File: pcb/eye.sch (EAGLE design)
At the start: 36 parts, among them U1 WS2812, U10 WS2812, U11 WS2812, U12 WS2812, U13 WS2812, U14 WS2812, U15 WS2812, U16 WS2812, U17 WS2812, U18 WS2812, U19 WS2812, U2 WS2812, U20 WS2812, U21 WS2812, U22 WS2812, U23 WS2812, U24 WS2812, U25 WS2812, U26 WS2812, U27 WS2812, U28 WS2812, U29 WS2812, U3 WS2812, U30 WS2812, U4 WS2812, U5 WS2812, U6 WS2812, U7 WS2812, U8 WS2812, U9 WS2812

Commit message: start route data lines
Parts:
- added J1, J2: 3-PIN SMD, SparkFun-Connectors:CONN_03JST-SMD
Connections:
- new net N$30: J1.2, U1.DI
- net +5V: now also J1.3, J2.3
- net GND: now also J1.1, J2.1
- net N$31: now also J2.2
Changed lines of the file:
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@@
 <part name="P+36" library="supply1" library_urn="urn:adsk.eagle:library:371" deviceset="+5V" device=""/>
 <part name="GND36" library="supply1" library_urn="urn:adsk.eagle:library:371" deviceset="GND" device=""/>
+<part name="J1" library="SparkFun-Connectors" library_urn="urn:adsk.eagle:library:513" deviceset="CONN_03" device="JST-SMD" package3d_urn="urn:adsk.eagle:package:38075/1" value="3-PIN SMD"/>
+<part name="P+37" library="supply1" library_urn="urn:adsk.eagle:library:371" deviceset="+5V" device=""/>
+<part name="GND37" library="supply1" library_urn="urn:adsk.eagle:library:371" deviceset="GND" device=""/>
+<part name="J2" library="SparkFun-Connectors" library_urn="urn:adsk.eagle:library:513" deviceset="CONN_03" device="JST-SMD" package3d_urn="urn:adsk.eagle:package:38075/1" value="3-PIN SMD"/>
+<part name="GND38" library="supply1" library_urn="urn:adsk.eagle:library:371" deviceset="GND" device=""/>
+<part name="P+38" library="supply1" library_urn="urn:adsk.eagle:library:371" deviceset="+5V" device=""/>
 </parts>
 <sheets>
@@
 <attribute name="VALUE" x="261.62" y="83.82" size="1.778" layer="96"/>
 </instance>
+<instance part="J1" gate="J$1" x="-10.16" y="215.9" smashed="yes">
+<attribute name="VALUE" x="-12.7" y="208.534" size="1.778" layer="96" font="vector"/>
+<attribute name="NAME" x="-12.7" y="221.488" size="1.778" layer="95" font="vector"/>
+</instance>
+<instance part="P+37" gate="1" x="5.08" y="220.98" smashed="yes">
+<attribute name="VALUE" x="5.08" y="220.98" size="1.778" layer="96"/>
+</instance>
+<instance part="GND37" gate="1" x="5.08" y="210.82" smashed="yes">
+<attribute name="VALUE" x="2.54" y="208.28" size="1.778" layer="96"/>
+</instance>
+<instance part="J2" gate="J$1" x="266.7" y="71.12" smashed="yes" rot="R180">
+<attribute name="VALUE" x="261.62" y="63.754" size="1.778" layer="96" font="vector"/>
+<attribute name="NAME" x="266.7" y="76.708" size="1.778" layer="95" font="vector"/>
+</instance>
+<instance part="GND38" gate="1" x="254" y="76.2" smashed="yes">
+<attribute name="VALUE" x="251.46" y="73.66" size="1.778" layer="96"/>
+</instance>
+<instance part="P+38" gate="1" x="254" y="68.58" smashed="yes">
+<attribute name="VALUE" x="254" y="68.58" size="1.778" layer="96"/>
+</instance>
 </instances>
 <busses>
@@
 <pinref part="P+36" gate="1" pin="+5V"/>
 </segment>
+<segment>
+<pinref part="J1" gate="J$1" pin="3"/>
+<pinref part="P+37" gate="1" pin="+5V"/>
+<wire x1="5.08" y1="218.44" x2="-2.54" y2="218.44" width="0.1524" layer="91"/>
+</segment>
+<segment>
+<pinref part="J2" gate="J$1" pin="3"/>
+<pinref part="P+38" gate="1" pin="+5V"/>
+<wire x1="254" y1="66.04" x2="259.08" y2="66.04" width="0.1524" layer="91"/>
+<wire x1="259.08" y1="66.04" x2="259.08" y2="68.58" width="0.1524" layer="91"/>
+</segment>
 </net>
 <net name="GND" class="0">
@@
 <pinref part="C6" gate="G$1" pin="2"/>
 <pinref part="GND36" gate="1" pin="GND"/>
+</segment>
+<segment>
+<pinref part="J1" gate="J$1" pin="1"/>
+<pinref part="GND37" gate="1" pin="GND"/>
+<wire x1="5.08" y1="213.36" x2="-2.54" y2="213.36" width="0.1524" layer="91"/>
+</segment>
+<segment>
+<pinref part="J2" gate="J$1" pin="1"/>
+<pinref part="GND38" gate="1" pin="GND"/>
+<wire x1="254" y1="78.74" x2="259.08" y2="78.74" width="0.1524" layer="91"/>
+<wire x1="259.08" y1="78.74" x2="259.08" y2="73.66" width="0.1524" layer="91"/>
 </segment>
 </net>
@@
 <segment>
 <pinref part="U30" gate="U1" pin="DO"/>
-<wire x1="248.92" y1="88.9" x2="248.92" y2="81.28" width="0.1524" layer="91"/>
-</segment>
-</net>
+<pinref part="J2" gate="J$1" pin="2"/>
+<wire x1="248.92" y1="88.9" x2="248.92" y2="71.12" width="0.1524" layer="91"/>
+<wire x1="248.92" y1="71.12" x2="259.08" y2="71.12" width="0.1524" layer="91"/>
+</segment>
+</net>
+<net name="N$30" class="0">
+<segment>
+<pinref part="J1" gate="J$1" pin="2"/>
+<pinref part="U1" gate="U1" pin="DI"/>
+<wire x1="-2.54" y1="215.9" x2="22.86" y2="215.9" width="0.1524" layer="91"/>
+</segment>
+</net>

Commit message: change connector to TE AMP 171826-3
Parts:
- removed J1, J2: 3-PIN SMD, SparkFun-Connectors:CONN_03JST-SMD
- added JP1, JP2: (no value), pinhead:PINHD-1X3/90
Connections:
- net +5V: now also JP1.3, JP2.3; no longer J1.3, J2.3
- net GND: now also JP1.1, JP2.1; no longer J1.1, J2.1
- net N$30: now also JP1.2; no longer J1.2
- net N$31: now also JP2.2; no longer J2.2
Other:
- note added: "AMP171826-3"
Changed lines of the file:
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@@
 <part name="P+36" library="supply1" library_urn="urn:adsk.eagle:library:371" deviceset="+5V" device=""/>
 <part name="GND36" library="supply1" library_urn="urn:adsk.eagle:library:371" deviceset="GND" device=""/>
-<part name="J1" library="SparkFun-Connectors" library_urn="urn:adsk.eagle:library:513" deviceset="CONN_03" device="JST-SMD" package3d_urn="urn:adsk.eagle:package:38075/1" value="3-PIN SMD"/>
 <part name="P+37" library="supply1" library_urn="urn:adsk.eagle:library:371" deviceset="+5V" device=""/>
 <part name="GND37" library="supply1" library_urn="urn:adsk.eagle:library:371" deviceset="GND" device=""/>
-<part name="J2" library="SparkFun-Connectors" library_urn="urn:adsk.eagle:library:513" deviceset="CONN_03" device="JST-SMD" package3d_urn="urn:adsk.eagle:package:38075/1" value="3-PIN SMD"/>
 <part name="GND38" library="supply1" library_urn="urn:adsk.eagle:library:371" deviceset="GND" device=""/>
 <part name="P+38" library="supply1" library_urn="urn:adsk.eagle:library:371" deviceset="+5V" device=""/>
+<part name="JP1" library="pinhead" library_urn="urn:adsk.eagle:library:325" deviceset="PINHD-1X3" device="/90" package3d_urn="urn:adsk.eagle:package:22459/2"/>
+<part name="JP2" library="pinhead" library_urn="urn:adsk.eagle:library:325" deviceset="PINHD-1X3" device="/90" package3d_urn="urn:adsk.eagle:package:22459/2"/>
 </parts>
 <sheets>
 <sheet>
 <plain>
+<text x="0" y="208.28" size="1.778" layer="91" rot="R90">AMP171826-3</text>
+<text x="271.78" y="63.5" size="1.778" layer="91" rot="R90">AMP171826-3</text>
 </plain>
 <instances>
@@
 <attribute name="VALUE" x="261.62" y="83.82" size="1.778" layer="96"/>
 </instance>
-<instance part="J1" gate="J$1" x="-10.16" y="215.9" smashed="yes">
-<attribute name="VALUE" x="-12.7" y="208.534" size="1.778" layer="96" font="vector"/>
-<attribute name="NAME" x="-12.7" y="221.488" size="1.778" layer="95" font="vector"/>
-</instance>
-<instance part="P+37" gate="1" x="5.08" y="220.98" smashed="yes">
-<attribute name="VALUE" x="5.08" y="220.98" size="1.778" layer="96"/>
-</instance>
-<instance part="GND37" gate="1" x="5.08" y="210.82" smashed="yes">
-<attribute name="VALUE" x="2.54" y="208.28" size="1.778" layer="96"/>
-</instance>
-<instance part="J2" gate="J$1" x="266.7" y="71.12" smashed="yes" rot="R180">
-<attribute name="VALUE" x="261.62" y="63.754" size="1.778" layer="96" font="vector"/>
-<attribute name="NAME" x="266.7" y="76.708" size="1.778" layer="95" font="vector"/>
+<instance part="P+37" gate="1" x="12.7" y="220.98" smashed="yes">
+<attribute name="VALUE" x="12.7" y="220.98" size="1.778" layer="96"/>
+</instance>
+<instance part="GND37" gate="1" x="12.7" y="210.82" smashed="yes">
+<attribute name="VALUE" x="10.16" y="208.28" size="1.778" layer="96"/>
 </instance>
 <instance part="GND38" gate="1" x="254" y="76.2" smashed="yes">
@@
 <instance part="P+38" gate="1" x="254" y="68.58" smashed="yes">
 <attribute name="VALUE" x="254" y="68.58" size="1.778" layer="96"/>
+</instance>
+<instance part="JP1" gate="A" x="2.54" y="215.9" smashed="yes" rot="R180">
+<attribute name="NAME" x="6.35" y="210.185" size="1.778" layer="95" rot="R180"/>
+<attribute name="VALUE" x="8.89" y="223.52" size="1.778" layer="96" rot="R180"/>
+</instance>
+<instance part="JP2" gate="A" x="266.7" y="71.12" smashed="yes">
+<attribute name="NAME" x="260.35" y="76.835" size="1.778" layer="95"/>
+<attribute name="VALUE" x="260.35" y="63.5" size="1.778" layer="96"/>
 </instance>
 </instances>
@@
 </segment>
 <segment>
-<pinref part="J1" gate="J$1" pin="3"/>
 <pinref part="P+37" gate="1" pin="+5V"/>
-<wire x1="5.08" y1="218.44" x2="-2.54" y2="218.44" width="0.1524" layer="91"/>
-</segment>
-<segment>
-<pinref part="J2" gate="J$1" pin="3"/>
+<wire x1="12.7" y1="218.44" x2="5.08" y2="218.44" width="0.1524" layer="91"/>
+<pinref part="JP1" gate="A" pin="3"/>
+</segment>
+<segment>
 <pinref part="P+38" gate="1" pin="+5V"/>
 <wire x1="254" y1="66.04" x2="259.08" y2="66.04" width="0.1524" layer="91"/>
 <wire x1="259.08" y1="66.04" x2="259.08" y2="68.58" width="0.1524" layer="91"/>
+<wire x1="259.08" y1="68.58" x2="264.16" y2="68.58" width="0.1524" layer="91"/>
+<pinref part="JP2" gate="A" pin="3"/>
 </segment>
 </net>
@@
 </segment>
 <segment>
-<pinref part="J1" gate="J$1" pin="1"/>
 <pinref part="GND37" gate="1" pin="GND"/>
-<wire x1="5.08" y1="213.36" x2="-2.54" y2="213.36" width="0.1524" layer="91"/>
-</segment>
-<segment>
-<pinref part="J2" gate="J$1" pin="1"/>
+<wire x1="12.7" y1="213.36" x2="5.08" y2="213.36" width="0.1524" layer="91"/>
+<pinref part="JP1" gate="A" pin="1"/>
+</segment>
+<segment>
 <pinref part="GND38" gate="1" pin="GND"/>
 <wire x1="254" y1="78.74" x2="259.08" y2="78.74" width="0.1524" layer="91"/>
 <wire x1="259.08" y1="78.74" x2="259.08" y2="73.66" width="0.1524" layer="91"/>
+<wire x1="259.08" y1="73.66" x2="264.16" y2="73.66" width="0.1524" layer="91"/>
+<pinref part="JP2" gate="A" pin="1"/>
 </segment>
 </net>
@@
 <segment>
 <pinref part="U30" gate="U1" pin="DO"/>
-<pinref part="J2" gate="J$1" pin="2"/>
 <wire x1="248.92" y1="88.9" x2="248.92" y2="71.12" width="0.1524" layer="91"/>
-<wire x1="248.92" y1="71.12" x2="259.08" y2="71.12" width="0.1524" layer="91"/>
+<wire x1="248.92" y1="71.12" x2="264.16" y2="71.12" width="0.1524" layer="91"/>
+<pinref part="JP2" gate="A" pin="2"/>
 </segment>
 </net>
 <net name="N$30" class="0">
 <segment>
-<pinref part="J1" gate="J$1" pin="2"/>
 <pinref part="U1" gate="U1" pin="DI"/>
-<wire x1="-2.54" y1="215.9" x2="22.86" y2="215.9" width="0.1524" layer="91"/>
-</segment>
-</net>
+<wire x1="5.08" y1="215.9" x2="22.86" y2="215.9" width="0.1524" layer="91"/>
+<pinref part="JP1" gate="A" pin="2"/>
+</segment>
+</net>

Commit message: make full glasses and add mcu to them
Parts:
- removed JP2: (no value), pinhead:PINHD-1X3/90
- added 32U4: 32U4, SparkFun-IC-Microcontroller:ATMEGA32U4QFN
- added C10, C11, C12, C7, C8, C9: (no value), rcl:C-EUC0805
- added C13, C14: 1u, rcl:C-EUC0805
- added C15, C16: 20p, rcl:C-EUC0805
- added J1: (no value), SparkFun-Connectors:USB_MICRO-B_FEMALE-SMT
- added Q1: ECS-160-20-3X-TR, SparkFun-Clocks:CRYSTALSMD-3.2X1.5
- added R1: 470, rcl:R-US_R0805
- added R2, R3: 22, rcl:R-US_R0805
- added R4: 1k, rcl:R-US_R0805
- added U31, U32, U33, U34, U35, U36, U37, U38, U39, U40, U41, U42, U43, U44, U45, U46, U47, U48, U49, U50, U51, U52, U53, U54, U55, U56, U57, U58, U59, U60: WS2812, SparkFun-LED:WS2812"
- JP1: value (none) -> JST-ZH-5; device pinhead:PINHD-1X3/90 -> josh:JST-ZH-5
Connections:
- new net LED_DATA: 32U4.PB7, R1.1
- new net N$32: U32.DO, U33.DI
- new net N$33: U33.DO, U34.DI
- new net N$34: U34.DO, U35.DI
- new net N$35: U35.DO, U36.DI
- new net N$36: U36.DO, U37.DI
- new net N$37: U37.DO, U38.DI
- new net N$38: U38.DO, U39.DI
- new net N$39: U39.DO, U40.DI
- new net N$40: U40.DO, U41.DI
- new net N$41: U41.DO, U42.DI
- new net N$42: U42.DO, U43.DI
- new net N$43: U43.DO, U44.DI
- new net N$44: U44.DO, U45.DI
- new net N$45: U45.DO, U46.DI
- new net N$46: U46.DO, U47.DI
- new net N$47: U47.DO, U48.DI
- new net N$48: U48.DO, U49.DI
- new net N$49: U49.DO, U50.DI
- new net N$50: U50.DO, U51.DI
- new net N$51: U51.DO, U52.DI
- new net N$52: U52.DO, U53.DI
- new net N$53: U53.DO, U54.DI
- new net N$54: U54.DO, U55.DI
- new net N$55: U55.DO, U56.DI
- new net N$56: U56.DO, U57.DI
- new net N$57: U57.DO, U58.DI
- new net N$58: U58.DO, U59.DI
- new net N$59: U59.DO, U60.DI
- new net N$60: U30.DO, U31.DI
- new net N$61: R1.2, U1.DI
- new net N$62: 32U4.UCAP, C13.1
- new net N$63: 32U4.PF1(ADC1), JP1.3
- new net N$64: 32U4.PF4(ADC4), JP1.2
- new net N$67: 32U4.XTAL2, C16.1, Q1.2
- new net N$68: 32U4.XTAL1, C15.1, Q1.1
- new net N$77: 32U4.PE2/!HWB, R4.2
- new net RST: 32U4.!RESET
- new net USB1_N: J1.D-, R2.1
- new net USB1_P: J1.D+, R3.1
- new net USB_N: 32U4.D-, R2.2
- new net USB_P: 32U4.D+, R3.2
- net +5V: now also 32U4.AREF, 32U4.AVCC@24, 32U4.UVCC, 32U4.VBUS, 32U4.VCC@14, C10.1, C11.1, C12.1, C14.1, C7.1, C8.1, C9.1, J1.VBUS, JP1.1, U31.VDD, U32.VDD, U33.VDD, U34.VDD, U35.VDD, U36.VDD, U37.VDD, U38.VDD, U39.VDD, U40.VDD, U41.VDD, U42.VDD, U43.VDD, U44.VDD, U45.VDD, U46.VDD, U47.VDD, U48.VDD, U49.VDD, U50.VDD, U51.VDD, U52.VDD, U53.VDD, U54.VDD, U55.VDD, U56.VDD, U57.VDD, U58.VDD, U59.VDD, U60.VDD; no longer JP1.3, JP2.3
- net GND: now also 32U4.GND, C10.2, C11.2, C12.2, C13.2, C14.2, C15.2, C16.2, C7.2, C8.2, C9.2, J1.GND, J1.SHIELD, JP1.5, R4.1, U31.VSS, U32.VSS, U33.VSS, U34.VSS, U35.VSS, U36.VSS, U37.VSS, U38.VSS, U39.VSS, U40.VSS, U41.VSS, U42.VSS, U43.VSS, U44.VSS, U45.VSS, U46.VSS, U47.VSS, U48.VSS, U49.VSS, U50.VSS, U51.VSS, U52.VSS, U53.VSS, U54.VSS, U55.VSS, U56.VSS, U57.VSS, U58.VSS, U59.VSS, U60.VSS; no longer JP1.1, JP2.1
- net N$30: now also 32U4.PF0(ADC0), JP1.4; no longer JP1.2, U1.DI
- net N$31: now also U31.DO, U32.DI; no longer JP2.2, U30.DO
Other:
- note removed: "AMP171826-3"

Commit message: finish up glasses
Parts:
- added C17, C18, C19: (no value), rcl:C-EUC0603
- added U$4, U$5: GLASSES_HINGE, josh:GLASSES_HINGE
- C1, C10, C11, C12, C13, C14, C15, C16, C2, C3, C4, C5, C6, C7, C8, C9: device rcl:C-EUC0805 -> rcl:C-EUC0603
- JP1: value JST-ZH-5 -> JST-ZH-5SMD-RA; device josh:JST-ZH-5 -> josh:JST-ZH-5SMD-RA
- R1, R2, R3, R4: device rcl:R-US_R0805 -> rcl:R-US_R0603
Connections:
- net +5V: now also C17.1, C18.1, C19.1
- net GND: now also C17.2, C18.2, C19.2, U$4.P$1, U$4.P$2, U$5.P$1, U$5.P$2

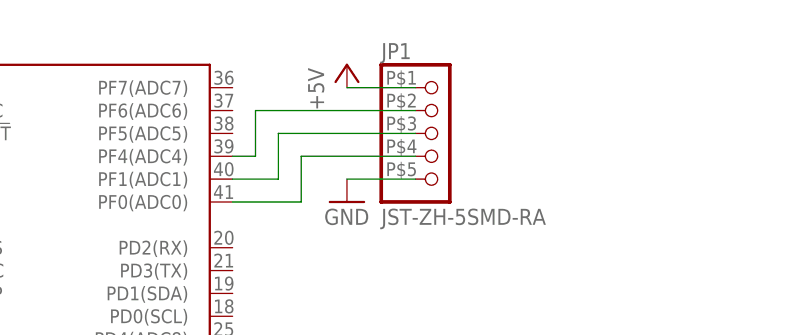
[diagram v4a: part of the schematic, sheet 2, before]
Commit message: update values and name placement
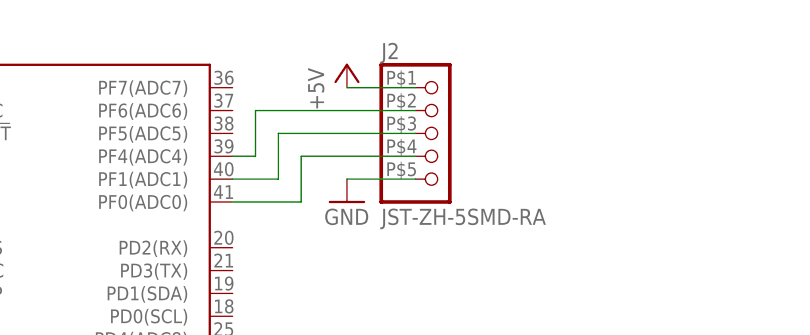
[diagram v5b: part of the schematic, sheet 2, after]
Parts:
- renumbered JP1 to J2
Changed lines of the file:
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@@
 <part name="P+37" library="supply1" library_urn="urn:adsk.eagle:library:371" deviceset="+5V" device=""/>
 <part name="GND37" library="supply1" library_urn="urn:adsk.eagle:library:371" deviceset="GND" device=""/>
-<part name="JP1" library="josh" deviceset="JST-ZH-5" device="SMD-RA" value="JST-ZH-5SMD-RA"/>
+<part name="J2" library="josh" deviceset="JST-ZH-5" device="SMD-RA" value="JST-ZH-5SMD-RA"/>
 <part name="U$4" library="josh" deviceset="GLASSES_HINGE" device=""/>
 <part name="U$5" library="josh" deviceset="GLASSES_HINGE" device=""/>
@@
 <attribute name="VALUE" x="101.6" y="71.12" size="1.778" layer="96"/>
 </instance>
-<instance part="JP1" gate="G$1" x="114.3" y="81.28" smashed="yes">
+<instance part="J2" gate="G$1" x="114.3" y="81.28" smashed="yes">
 <attribute name="NAME" x="107.95" y="89.535" size="1.778" layer="95"/>
 <attribute name="VALUE" x="107.95" y="71.12" size="1.778" layer="96"/>
@@
 <pinref part="P+37" gate="1" pin="+5V"/>
 <wire x1="104.14" y1="86.36" x2="111.76" y2="86.36" width="0.1524" layer="91"/>
-<pinref part="JP1" gate="G$1" pin="1"/>
+<pinref part="J2" gate="G$1" pin="1"/>
 </segment>
 <segment>
@@
 <pinref part="GND37" gate="1" pin="GND"/>
 <wire x1="104.14" y1="76.2" x2="111.76" y2="76.2" width="0.1524" layer="91"/>
-<pinref part="JP1" gate="G$1" pin="5"/>
+<pinref part="J2" gate="G$1" pin="5"/>
 </segment>
 <segment>
@@
 <pinref part="32U4" gate="U1" pin="PF0(ADC0)"/>
 <wire x1="91.44" y1="73.66" x2="99.06" y2="73.66" width="0.1524" layer="91"/>
-<pinref part="JP1" gate="G$1" pin="4"/>
+<pinref part="J2" gate="G$1" pin="4"/>
 <wire x1="99.06" y1="73.66" x2="99.06" y2="78.74" width="0.1524" layer="91"/>
 <wire x1="99.06" y1="78.74" x2="111.76" y2="78.74" width="0.1524" layer="91"/>
@@
 <wire x1="91.44" y1="76.2" x2="96.52" y2="76.2" width="0.1524" layer="91"/>
 <wire x1="96.52" y1="76.2" x2="96.52" y2="81.28" width="0.1524" layer="91"/>
-<pinref part="JP1" gate="G$1" pin="3"/>
+<pinref part="J2" gate="G$1" pin="3"/>
 <wire x1="96.52" y1="81.28" x2="111.76" y2="81.28" width="0.1524" layer="91"/>
 </segment>
@@
 <pinref part="32U4" gate="U1" pin="PF4(ADC4)"/>
 <wire x1="91.44" y1="78.74" x2="93.98" y2="78.74" width="0.1524" layer="91"/>
-<pinref part="JP1" gate="G$1" pin="2"/>
+<pinref part="J2" gate="G$1" pin="2"/>
 <wire x1="93.98" y1="78.74" x2="93.98" y2="83.82" width="0.1524" layer="91"/>
 <wire x1="93.98" y1="83.82" x2="111.76" y2="83.82" width="0.1524" layer="91"/>
